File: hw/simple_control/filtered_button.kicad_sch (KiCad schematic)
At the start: 4 parts, among them SW1201 SW_Push

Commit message: chore(hw): assign footprints
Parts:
- C1201: footprint (none) -> Capacitor_SMD:C_0805_2012Metric_Pad1.18x1.45mm_HandSolder
- R1201, R1202: footprint (none) -> Resistor_SMD:R_0805_2012Metric_Pad1.20x1.40mm_HandSolder
- SW1201: footprint (none) -> Button_Switch_THT:SW_PUSH_6mm
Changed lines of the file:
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@@
       (effects (font (size 1.27 1.27)))
     )
-    (property "Footprint" "" (at 139.7 96.52 0)
+    (property "Footprint" "Button_Switch_THT:SW_PUSH_6mm" (at 139.7 96.52 0)
       (effects (font (size 1.27 1.27)) hide)
     )
@@
       (effects (font (size 1.27 1.27)) (justify left))
     )
-    (property "Footprint" "" (at 125.222 110.49 90)
+    (property "Footprint" "Resistor_SMD:R_0805_2012Metric_Pad1.20x1.40mm_HandSolder" (at 125.222 110.49 90)
       (effects (font (size 1.27 1.27)) hide)
     )
@@
       (effects (font (size 1.27 1.27)))
     )
-    (property "Footprint" "" (at 143.51 119.6848 0)
+    (property "Footprint" "Capacitor_SMD:C_0805_2012Metric_Pad1.18x1.45mm_HandSolder" (at 143.51 119.6848 0)
       (effects (font (size 1.27 1.27)) hide)
     )
@@
       (effects (font (size 1.27 1.27)) (justify left))
     )
-    (property "Footprint" "" (at 125.222 92.71 90)
+    (property "Footprint" "Resistor_SMD:R_0805_2012Metric_Pad1.20x1.40mm_HandSolder" (at 125.222 92.71 90)
       (effects (font (size 1.27 1.27)) hide)
     )

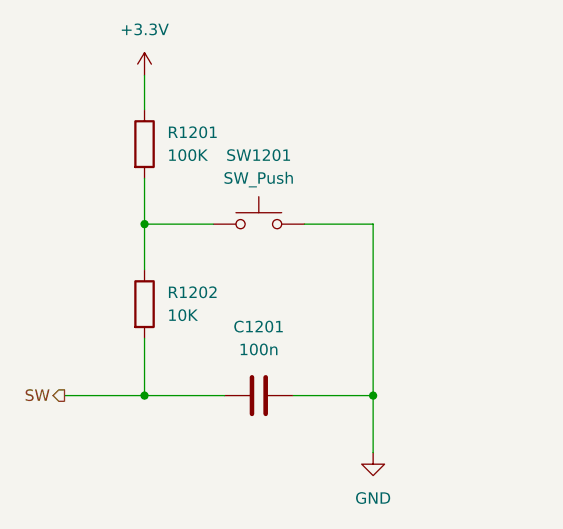
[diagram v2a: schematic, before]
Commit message: chore(hw): add mounting holes and connect power planes
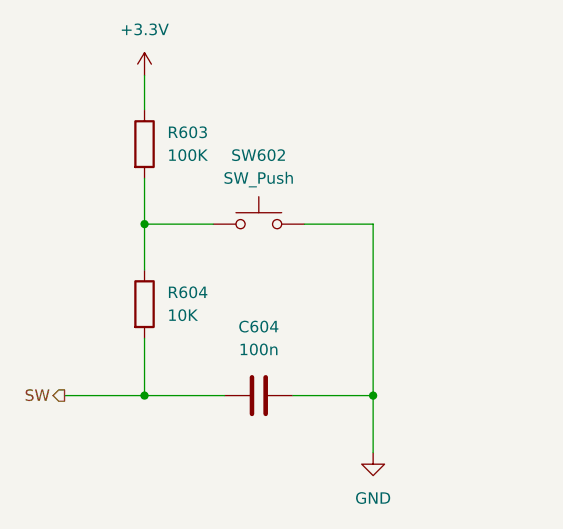
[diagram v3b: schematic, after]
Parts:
- renumbered C1201 to C604, R1201 to R603, R1202 to R604, SW1201 to SW602
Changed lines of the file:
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@@
   (symbol (lib_id "power:GND") (at 152.4 127 0) (unit 1)
     (in_bom yes) (on_board yes) (dnp no) (fields_autoplaced)
-    (property "Reference" "#PWR01202" (at 152.4 133.35 0)
+    (property "Reference" "#PWR0621" (at 152.4 133.35 0)
       (effects (font (size 1.27 1.27)) hide)
     )
@@
   (symbol (lib_id "Switch:SW_Push") (at 139.7 101.6 0) (unit 1)
     (in_bom yes) (on_board yes) (dnp no) (fields_autoplaced)
-    (property "Reference" "SW1201" (at 139.7 93.98 0)
+    (property "Reference" "SW602" (at 139.7 93.98 0)
       (effects (font (size 1.27 1.27)))
     )
@@
   (symbol (lib_id "Device:R") (at 127 110.49 0) (unit 1)
     (in_bom yes) (on_board yes) (dnp no) (fields_autoplaced)
-    (property "Reference" "R1202" (at 129.54 109.22 0)
+    (property "Reference" "R604" (at 129.54 109.22 0)
       (effects (font (size 1.27 1.27)) (justify left))
     )
@@
   (symbol (lib_id "Device:C") (at 139.7 120.65 90) (unit 1)
     (in_bom yes) (on_board yes) (dnp no) (fields_autoplaced)
-    (property "Reference" "C1201" (at 139.7 113.03 90)
+    (property "Reference" "C604" (at 139.7 113.03 90)
       (effects (font (size 1.27 1.27)))
     )
@@
   (symbol (lib_id "Device:R") (at 127 92.71 0) (unit 1)
     (in_bom yes) (on_board yes) (dnp no) (fields_autoplaced)
-    (property "Reference" "R1201" (at 129.54 91.44 0)
+    (property "Reference" "R603" (at 129.54 91.44 0)
       (effects (font (size 1.27 1.27)) (justify left))
     )
@@
   (symbol (lib_id "power:+3.3V") (at 127 85.09 0) (unit 1)
     (in_bom yes) (on_board yes) (dnp no) (fields_autoplaced)
-    (property "Reference" "#PWR01201" (at 127 88.9 0)
+    (property "Reference" "#PWR0620" (at 127 88.9 0)
       (effects (font (size 1.27 1.27)) hide)
     )

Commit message: chore(hw): add buttons layout
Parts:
- renumbered C604 to C1801, R603 to R1801, R604 to R1802, SW602 to SW1801
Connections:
- net GND: now also C1801.1, SW1801.1; no longer C1801.2, SW1801.2
- net SW: now also C1801.2; no longer C1801.1
- net at R1801.2, R1802.1: now also SW1801.2; no longer SW1801.1
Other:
- moved on the sheet: C1801, R1802, SW1801
